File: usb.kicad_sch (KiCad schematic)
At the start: 144 parts, among them J1 USB4105-GF-A, J4 WE_632723300011_alt_symbol, U3 TUSB1046-DCI, U4 CY7C65632-28LTXCT

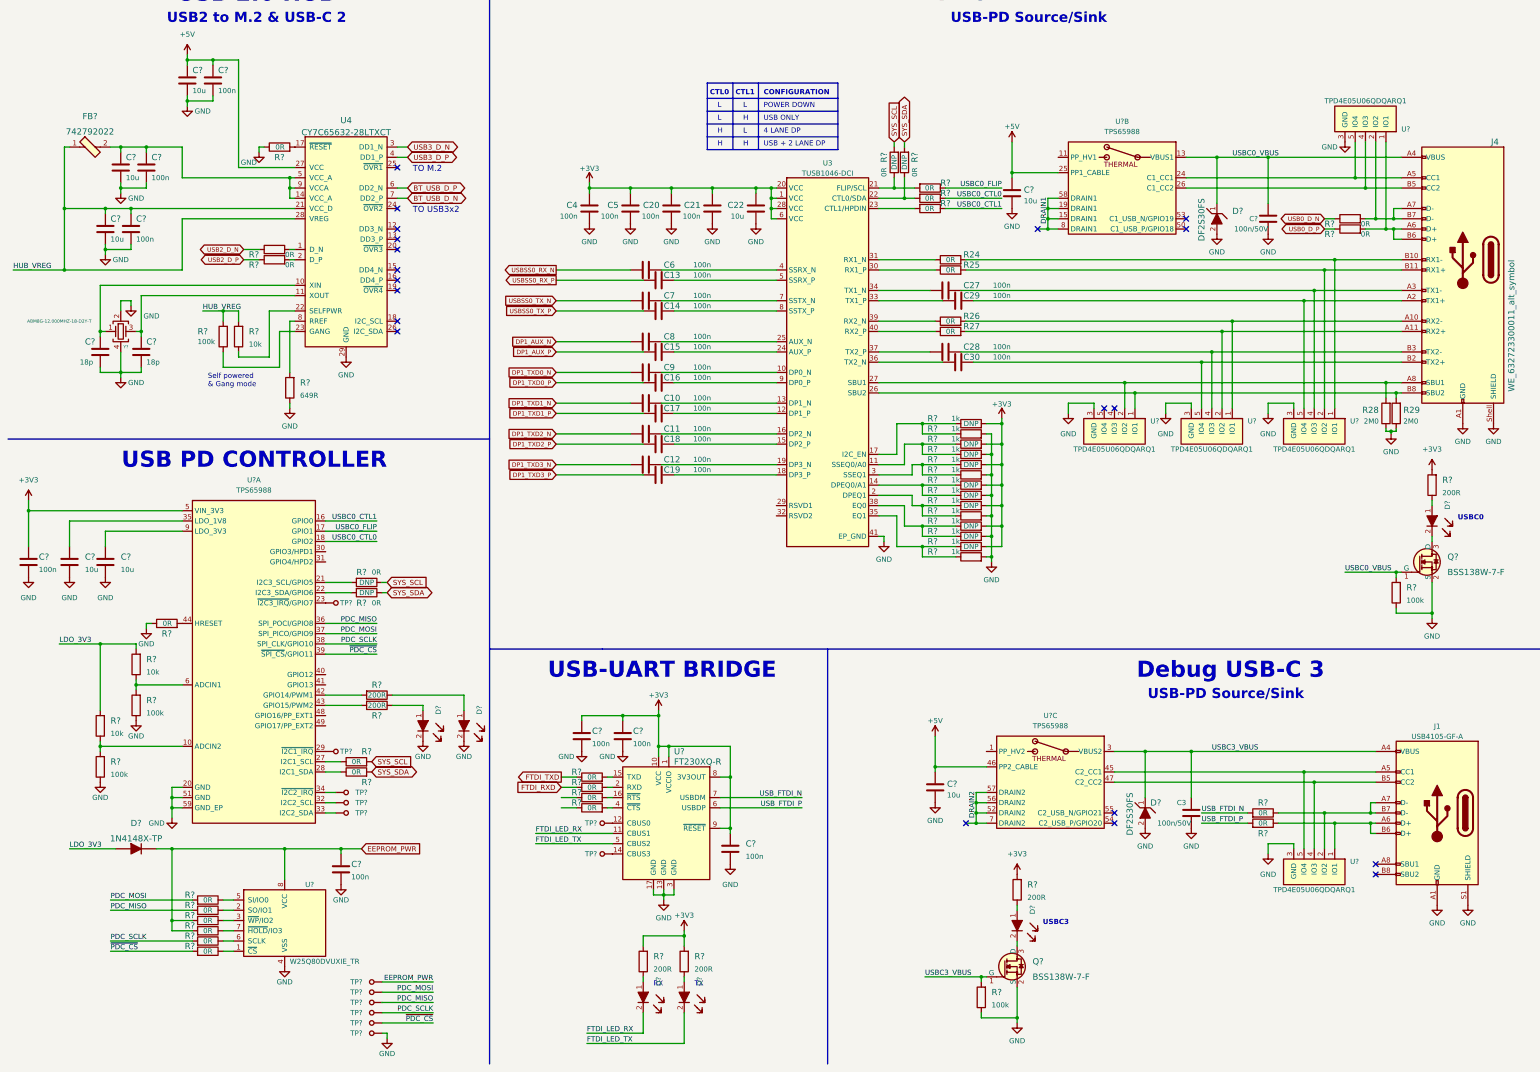
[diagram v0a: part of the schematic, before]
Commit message: Add labels to majority of the wires and fix minor errors in usb.kicad_sch
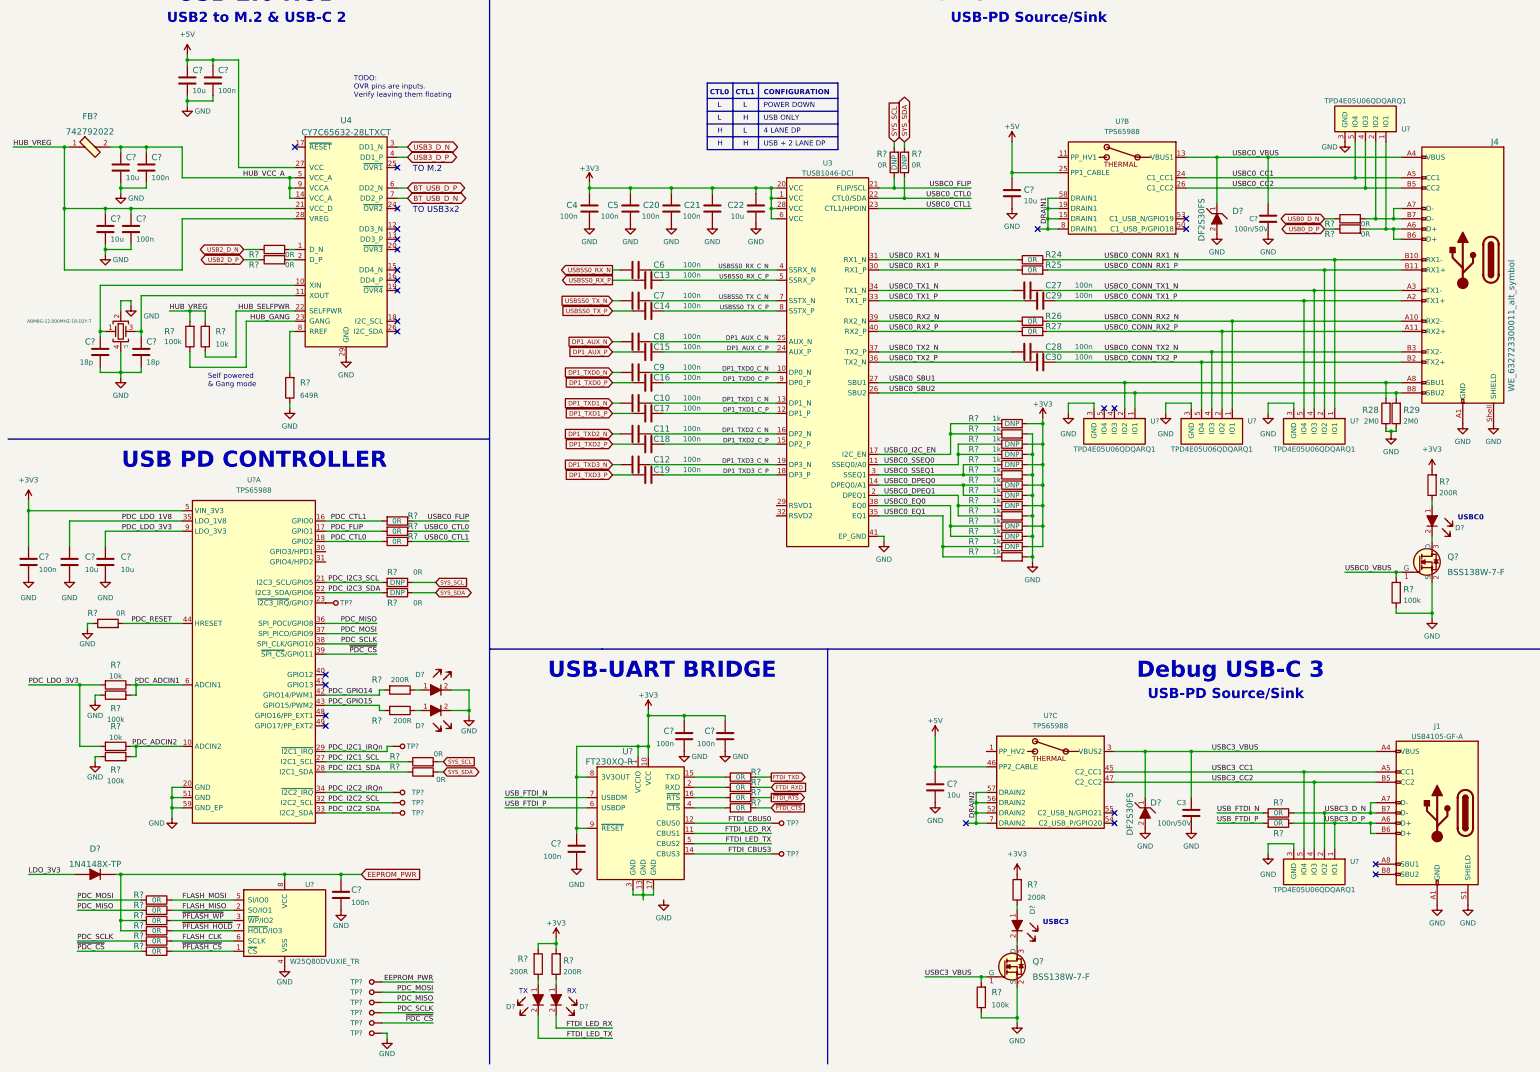
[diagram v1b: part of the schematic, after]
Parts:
- removed R?: R_0R_0402, antmicro-footprints:0402-res, symbol antmicroResistors0402:R_0R_0402
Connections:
- net GND: no longer U?.13 (GND), U?.17 (GND), U?.3 (GND)
- net LDO_3V3: no longer R?.2, R?.2
- net USBC0_CTL0: now also R?.1, U3.22 (CTL0/SDA); no longer U?.18 (GPIO2)
- net USBC0_CTL1: now also U3.23 (CTL1/HPDIN); no longer U?.16 (GPIO0)
- net USBC0_FLIP: now also R?.1, U3.21 (FLIP/SCL); no longer U?.17 (GPIO1)
- net DP1_TXD1_C_P: now reaches C17.2, U3.12 (DP1_P)
- net USBC0_CONN_RX2_N: now reaches J4.A10 (RX2-), R26.2, U?.1 (IO1), U?.10 (IO1)
- net USBC0_CONN_RX2_P: now reaches J4.A11 (RX2+), R27.2, U?.2 (IO2), U?.9 (IO2)
- net USBC0_CONN_TX2_N: now reaches C28.2, J4.B3 (TX2-), U?.4 (IO3), U?.7 (IO3)
- net USBC0_CONN_TX2_P: now reaches C30.2, J4.B2 (TX2+), U?.5 (IO4), U?.6 (IO4)
- net ~{FTDI_RTS}: now reaches R?.1
- net USBC0_SSEQ0: now reaches R?.1, R?.1, U3.11 (SSEQ0/A0)
- net USBC0_RX1_N: now reaches R24.1, U3.31 (RX1_N)
- net USBC0_CONN_RX1_N: now reaches J4.B10 (RX1-), R24.2, U?.1 (IO1), U?.10 (IO1)
- net PDC_ADCIN2: now reaches R?.1, R?.2, U?.10 (ADCIN2)
- net USBC0_EQ1: now reaches R?.1, R?.1, U3.35 (EQ1)
- net USBC0_RX1_P: now reaches R25.1, U3.30 (RX1_P)
- net USBC0_CONN_RX1_P: now reaches J4.B11 (RX1+), R25.2, U?.2 (IO2), U?.9 (IO2)
- net DP1_TXD3_C_P: now reaches C19.2, U3.18 (DP3_P)
- net FTDI_CBUS0: now reaches TP?.1, U?.12 (CBUS0)
- net FLASH_CLK: now reaches R?.1, U?.6 (SCLK)
- net USBC0_CC1: now reaches J4.A5 (CC1), U?.24 (C1_CC1), U?.5 (IO4), U?.6 (IO4)
- net USBC0_CC2: now reaches J4.B5 (CC2), U?.26 (C1_CC2), U?.4 (IO3), U?.7 (IO3)
- net USBC0_DPEQ1: now reaches R?.1, R?.1, U3.2 (DPEQ1)
- net USBC0_SSEQ1: now reaches R?.1, R?.1, U3.3 (SSEQ1)
- net USBC0_DPEQ0: now reaches R?.1, R?.1, U3.14 (DPEQ0/A1)
- net PDC_I2C2_IRQn: now reaches TP?.1, U?.34 (~{I2C2_IRQ})
- net HUB_VCC_A: now reaches C?.1, C?.1, FB?.2, U4.14 (VCC_A), U4.5 (VCC_A), U4.9 (VCCA)
- net HUB_SELFPWR: now reaches R?.1, U4.22 (SELFPWR)
- net HUB_GANG: now reaches R?.1, U4.23 (GANG)
- net PDC_LDO_1V8: now reaches C?.1, U?.35 (LDO_1V8)
- net USBSS0_RX_C_N: now reaches C6.2, U3.4 (SSRX_N)
- net USBSS0_TX_C_P: now reaches C14.2, U3.8 (SSTX_P)
- net USBC3_CC1: now reaches J1.A5 (CC1), U?.45 (C2_CC1), U?.5 (IO4), U?.6 (IO4)
- net USBC3_CC2: now reaches J1.B5 (CC2), U?.4 (IO3), U?.47 (C2_CC2), U?.7 (IO3)
- net FLASH_MOSI: now reaches R?.1, U?.5 (SI/IO0)
- net USBC0_TX2_N: now reaches C28.1, U3.37 (TX2_P)
- net DP1_AUX_C_N: now reaches C8.2, U3.25 (AUX_N)
- net DP1_TXD3_C_N: now reaches C12.2, U3.19 (DP3_N)
- net USBC0_EQ0: now reaches R?.1, R?.1, U3.38 (EQ0)
- net DP1_TXD1_C_N: now reaches C10.2, U3.13 (DP1_N)
- net USBC0_SBU1: now reaches J4.A8 (SBU1), R28.2, U3.27 (SBU1), U?.2 (IO2), U?.9 (IO2)
- net PDC_ADCIN1: now reaches R?.1, R?.2, U?.6 (ADCIN1)
- net PDC_GPIO15: now reaches R?.2, U?.43 (GPIO15/PWM2)
- net USBC0_I2C_EN: now reaches R?.1, R?.1, U3.17 (I2C_EN)
- net PDC_I2C3_SCL: now reaches R?.2, U?.21 (I2C3_SCL/GPIO5)
- net PDC_I2C3_SDA: now reaches R?.2, U?.22 (I2C3_SDA/GPIO6)
- net PDC_I2C1_SCL: now reaches R?.1, U?.27 (I2C1_SCL)
- net PDC_I2C1_SDA: now reaches R?.1, U?.28 (I2C1_SDA)
- net PDC_I2C1_IRQn: now reaches TP?.1, U?.29 (~{I2C1_IRQ})
- net PDC_I2C2_SCL: now reaches TP?.1, U?.32 (I2C2_SCL)
- net PDC_I2C2_SDA: now reaches TP?.1, U?.33 (I2C2_SDA)
- net PDC_GPIO14: now reaches R?.2, U?.42 (GPIO14/PWM1)
- net PDC_RESET: now reaches R?.2, U?.44 (HRESET)
- net PDC_LDO_3V3: now reaches C?.1, U?.9 (LDO_3V3)
- net PDC_LDO_3V3: now also R?.2, R?.2
- net USBC3_D_N: now reaches J1.A6 (D+), J1.B6 (D+), R?.1, U?.1 (IO1), U?.10 (IO1)
- net USBC3_D_N: now also J1.A7 (D-), J1.B7 (D-), R?.1, U?.2 (IO2), U?.9 (IO2)
- net ~{PFLASH_WP}: now reaches R?.1, U?.3 (~{WP}/IO2)
- net USBSS0_TX_C_N: now reaches C7.2, U3.7 (SSTX_N)
- net DP1_TXD0_C_N: now reaches C9.2, U3.10 (DP0_N)
- net DP1_TXD2_C_P: now reaches C18.2, U3.15 (DP2_P)
- net DP1_TXD2_C_N: now reaches C11.2, U3.16 (DP2_N)
- net PDC_CTL0: now reaches R?.2
- net PDC_CTL0: now also U?.18 (GPIO2); no longer U3.23 (CTL1/HPDIN)
- net DP1_AUX_C_P: now reaches C15.2, U3.24 (AUX_P)
- net USBC0_SBU2: now reaches J4.B8 (SBU2), R29.2, U3.26 (SBU2), U?.1 (IO1), U?.10 (IO1)
- net USBC0_TX1_P: now reaches C29.1, U3.33 (TX1_P)
- net USBC0_TX1_N: now reaches C27.1, U3.34 (TX1_N)
- net USBC0_TX2_P: now reaches C30.1, U3.36 (TX2_N)
- net USBC0_RX2_N: now reaches R26.1, U3.39 (RX2_N)
- net USBC0_RX2_P: now reaches R27.1, U3.40 (RX2_P)
- net USBSS0_RX_C_P: now reaches C13.2, U3.5 (SSRX_P)
- net DP1_TXD0_C_P: now reaches C16.2, U3.9 (DP0_P)
- net USBC0_CONN_TX1_N: now reaches C27.2, J4.A3 (TX1-), U?.4 (IO3), U?.7 (IO3)
- net ~{PFLASH_CS}: now reaches R?.1, U?.1 (~{CS})
- net FLASH_MISO: now reaches R?.1, U?.2 (SO/IO1)
- net ~{PFLASH_HOLD}: now reaches R?.1, U?.7 (~{HOLD}/IO3)
- net USBC0_CONN_TX1_P: now reaches C29.2, J4.A2 (TX1+), U?.5 (IO4), U?.6 (IO4)
- net FTDI_CBUS3: now reaches TP?.1, U?.14 (CBUS3)
- net ~{FTDI_CTS}: now reaches R?.1
- new net: U?.13 (GND), U?.17 (GND), U?.3 (GND)
- new net PDC_CTL1: R?.2, U?.16 (GPIO0)
- new net PDC_FLIP: R?.2, U?.17 (GPIO1)
- no-connect marks 20 -> 25
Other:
- note added: "TODO: OVR pins are inputs. Verify leaving them floating"
- moved on the sheet: C10, C11, C12, C13, C14, C15, C16, C17, C18, C19, C27, C28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

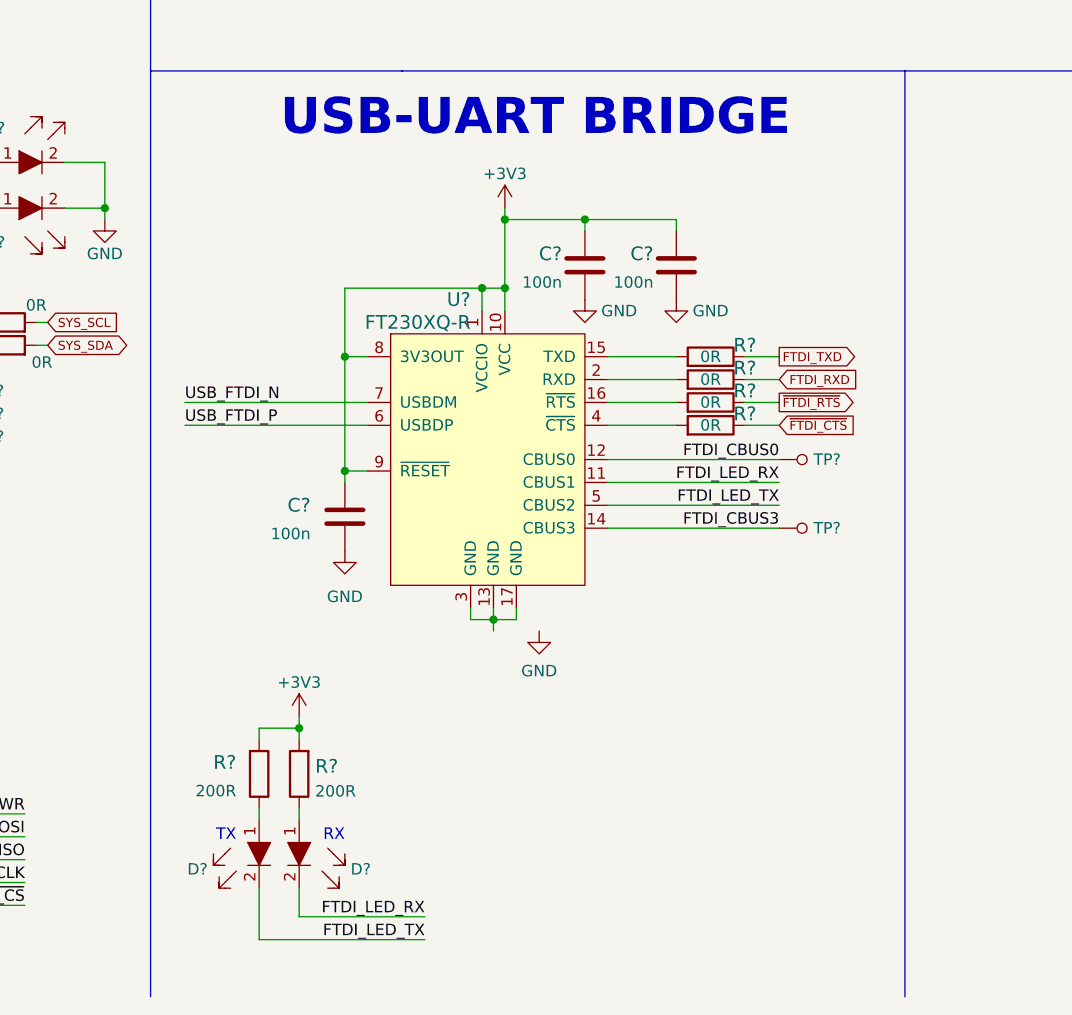
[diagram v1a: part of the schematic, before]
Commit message: Add LDO to supply FTDI
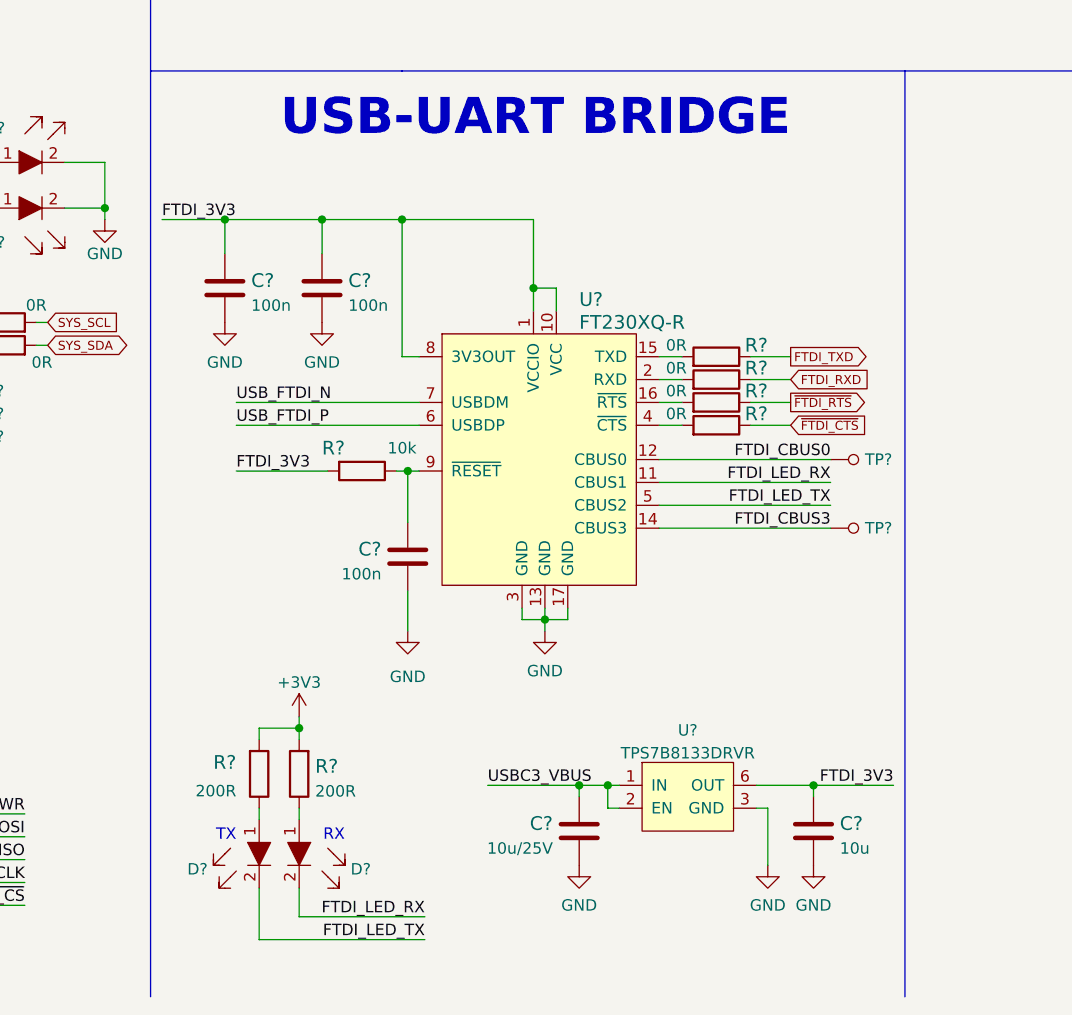
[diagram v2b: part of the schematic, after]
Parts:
- added C?: C_10u_25V_0603, antmicro-footprints:0603-cap, symbol antmicroCapacitors0603:C_10u_25V_0603
- added C?: C_10u_0402, antmicro-footprints:0402-cap, symbol antmicroCapacitors0402:C_10u_0402
- added R?: R_10k_0402, antmicro-footprints:0402-res, symbol antmicroResistors0402:R_10k_0402
- added U?: TPS7B8133DRVR, antmicro-footprints:WSON6_TI_2x2mm, symbol antmicroPMICVoltageRegulatorsLinear:TPS7B8133DRVR
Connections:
- net +3V3: no longer C?.1, C?.1, C?.1, U?.1 (VCCIO), U?.10 (VCC), U?.8 (3V3OUT), U?.9 (~{RESET})
- net GND: now also U?.13 (GND), U?.17 (GND), U?.3 (GND), C?.2, C?.2, U?.3 (GND), U?.4 (GND), U?.7 (GND)
- net USBC3_VBUS: now also C?.1, U?.1 (IN), U?.2 (EN)
- new net: C?.1, R?.1, U?.9 (~{RESET})
- new net FTDI_3V3: C?.1, C?.1, C?.1, R?.2, U?.1 (VCCIO), U?.10 (VCC), U?.6 (OUT), U?.8 (3V3OUT)
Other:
- moved on the sheet: C?, R?, TP?, U?

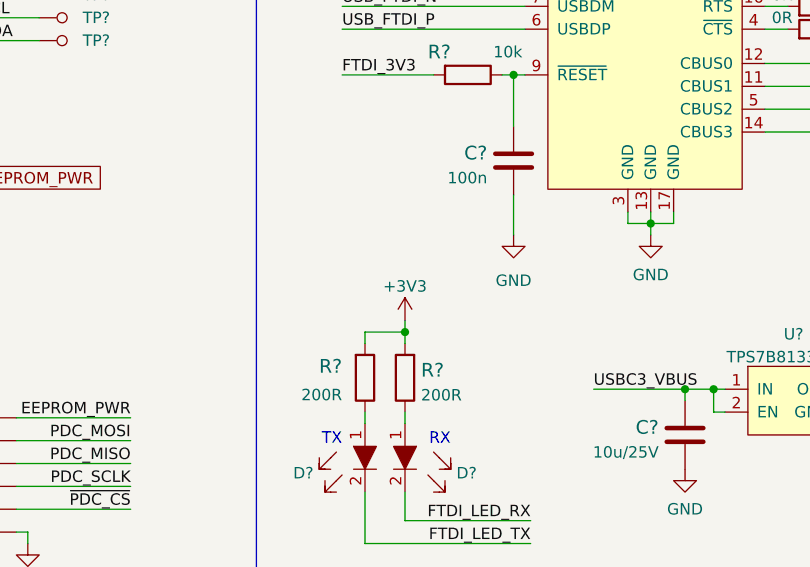
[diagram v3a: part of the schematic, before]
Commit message: Fixed FTDI LED power supply
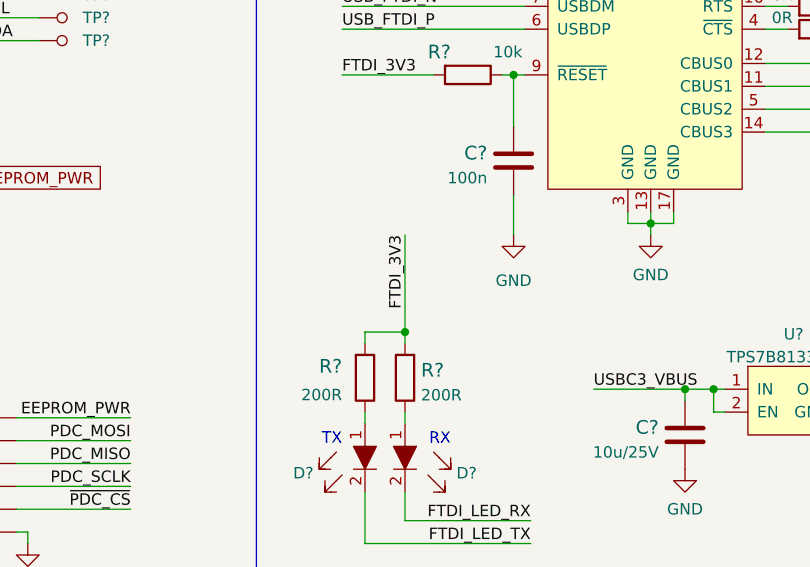
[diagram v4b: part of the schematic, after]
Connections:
- net +3V3: no longer R?.2, R?.2
- net FTDI_3V3: now also R?.2, R?.2
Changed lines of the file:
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@@
     (stroke (width 0) (type solid) (color 0 0 0 0))
   )
+  (wire (pts (xy 148.59 243.84) (xy 148.59 254.635))
+    (stroke (width 0) (type default) (color 0 0 0 0))
+  )
   (wire (pts (xy 119.38 209.55) (xy 120.65 209.55))
     (stroke (width 0) (type default) (color 0 0 0 0))
@@
     (stroke (width 0) (type default) (color 0 0 0 0))
   )
-  (wire (pts (xy 148.59 253.365) (xy 148.59 254.635))
-    (stroke (width 0) (type default) (color 0 0 0 0))
-  )
   (wire (pts (xy 30.48 190.5) (xy 30.48 205.74))
     (stroke (width 0) (type default) (color 0 0 0 0))
@@
     (effects (font (size 1.27 1.27)) (justify right bottom))
   )
+  (label "FTDI_3V3" (at 148.59 243.84 270)
+    (effects (font (size 1.27 1.27)) (justify right bottom))
+  )
   (label "USBC0_EQ0" (at 229.87 146.05 0)
     (effects (font (size 1.27 1.27)) (justify left bottom))
@@
     (pin "2")
   )
-  (symbol (lib_id "power:+3V3") (at 148.59 253.365 0) (mirror y) (unit 1)
-    (in_bom yes) (on_board yes)
-    (property "Reference" "#PWR?" (id 0) (at 148.59 257.175 0)
-      (effects (font (size 1.27 1.27)) hide)
-    )
-    (property "Value" "+3V3" (id 1) (at 148.59 249.555 0))
-    (property "Footprint" "" (id 2) (at 148.59 253.365 0)
-      (effects (font (size 1.27 1.27)) hide)
-    )
-    (property "Datasheet" "" (id 3) (at 148.59 253.365 0)
-      (effects (font (size 1.27 1.27)) hide)
-    )
-    (pin "1")
-  )
   (symbol (lib_id "antmicroCapacitors0402:C_10u_0402") (at 261.62 68.58 0) (unit 1)
